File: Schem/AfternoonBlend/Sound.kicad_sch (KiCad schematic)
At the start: 56 parts, among them J4 STX-3120-3B, J5 Conn_01x03, U10 LM4880MX/NOPB, U11 SN76489AN, U12 SN76489AN, U2 TLV2372, U3 AD7801BRUZ, U6 SN76489AN, U7 SN76489AN, U8 74HC138, U9 74HCT21, Y1 ECS-2100A-035

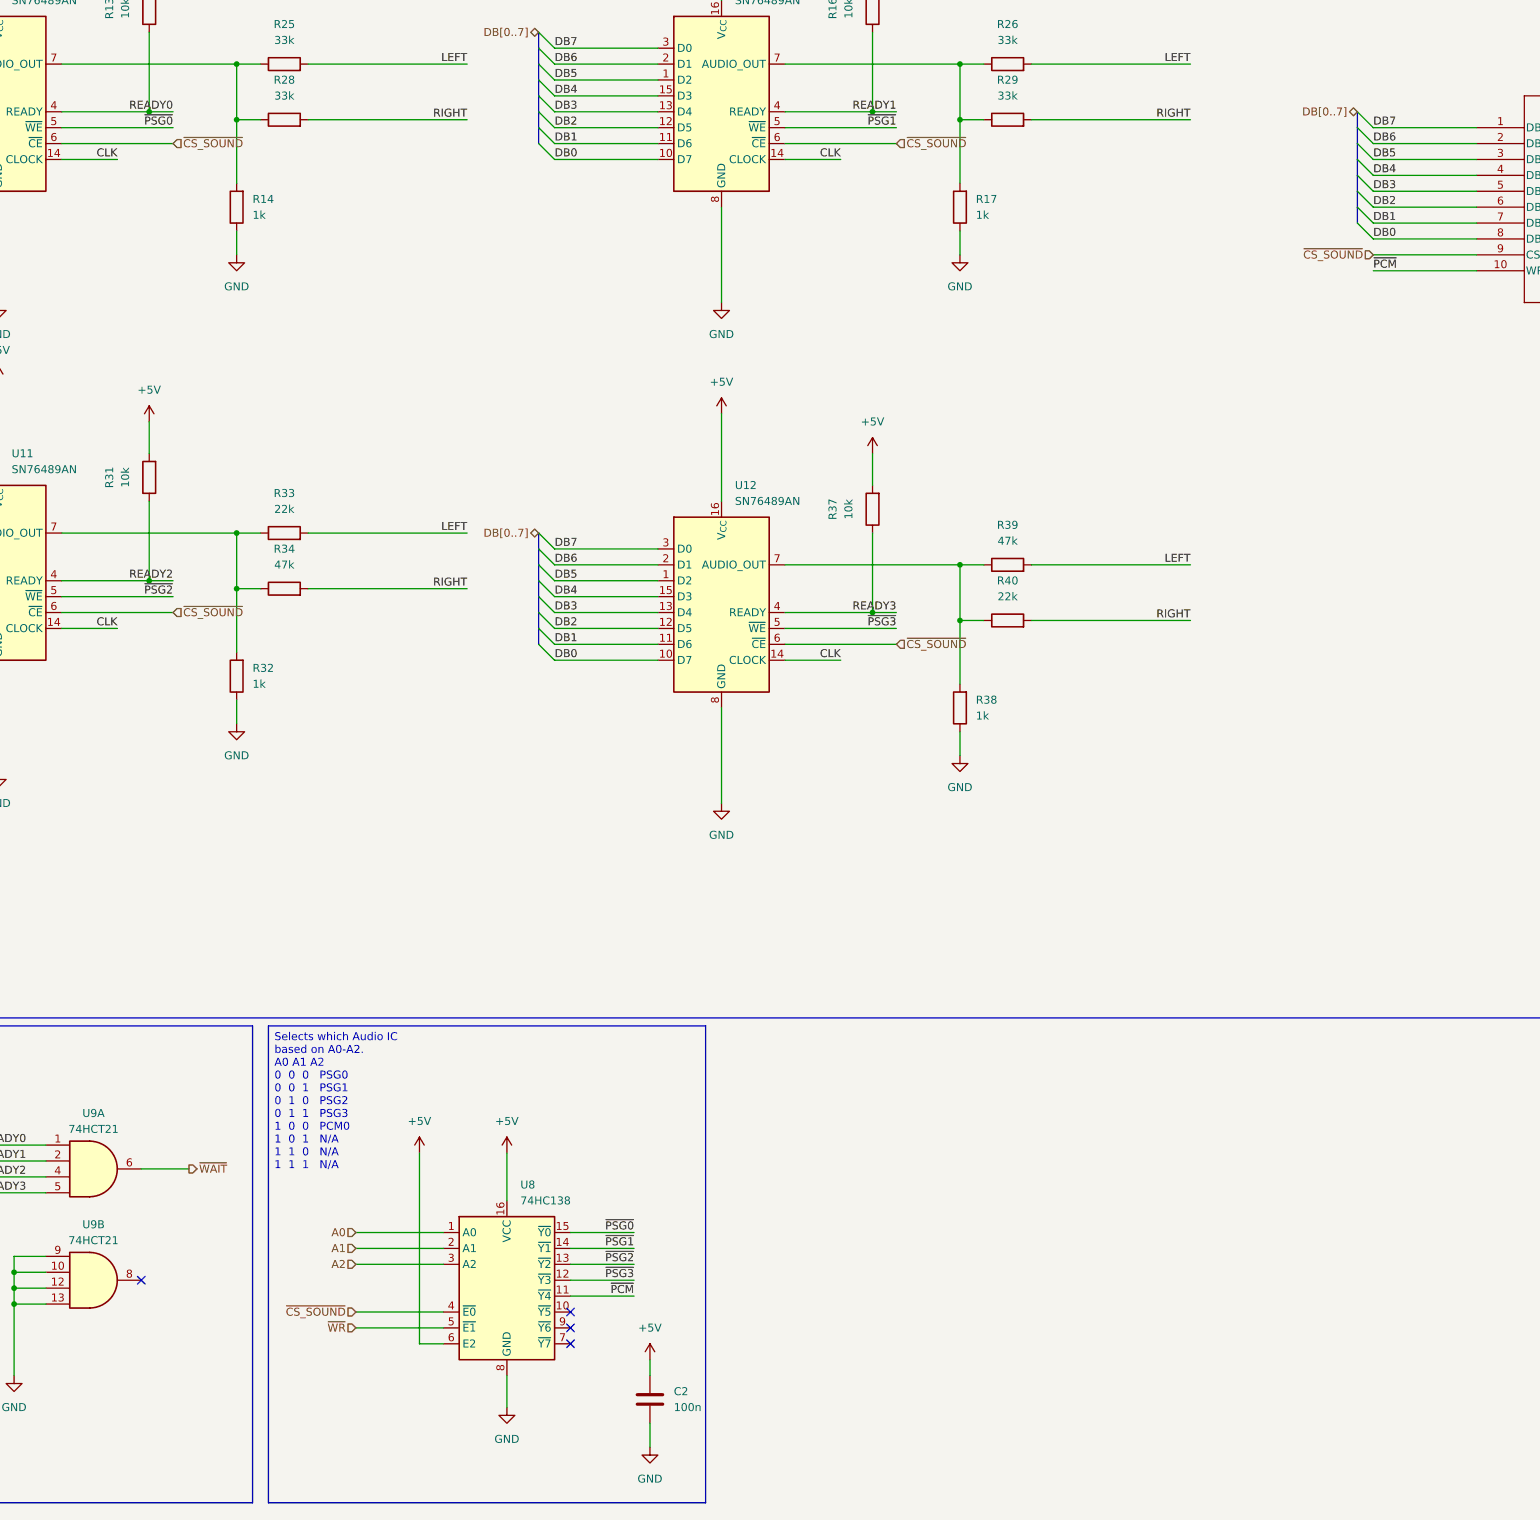
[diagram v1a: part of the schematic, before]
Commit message: Put back /CS_SOUND as the qualifying signal instead of /WR
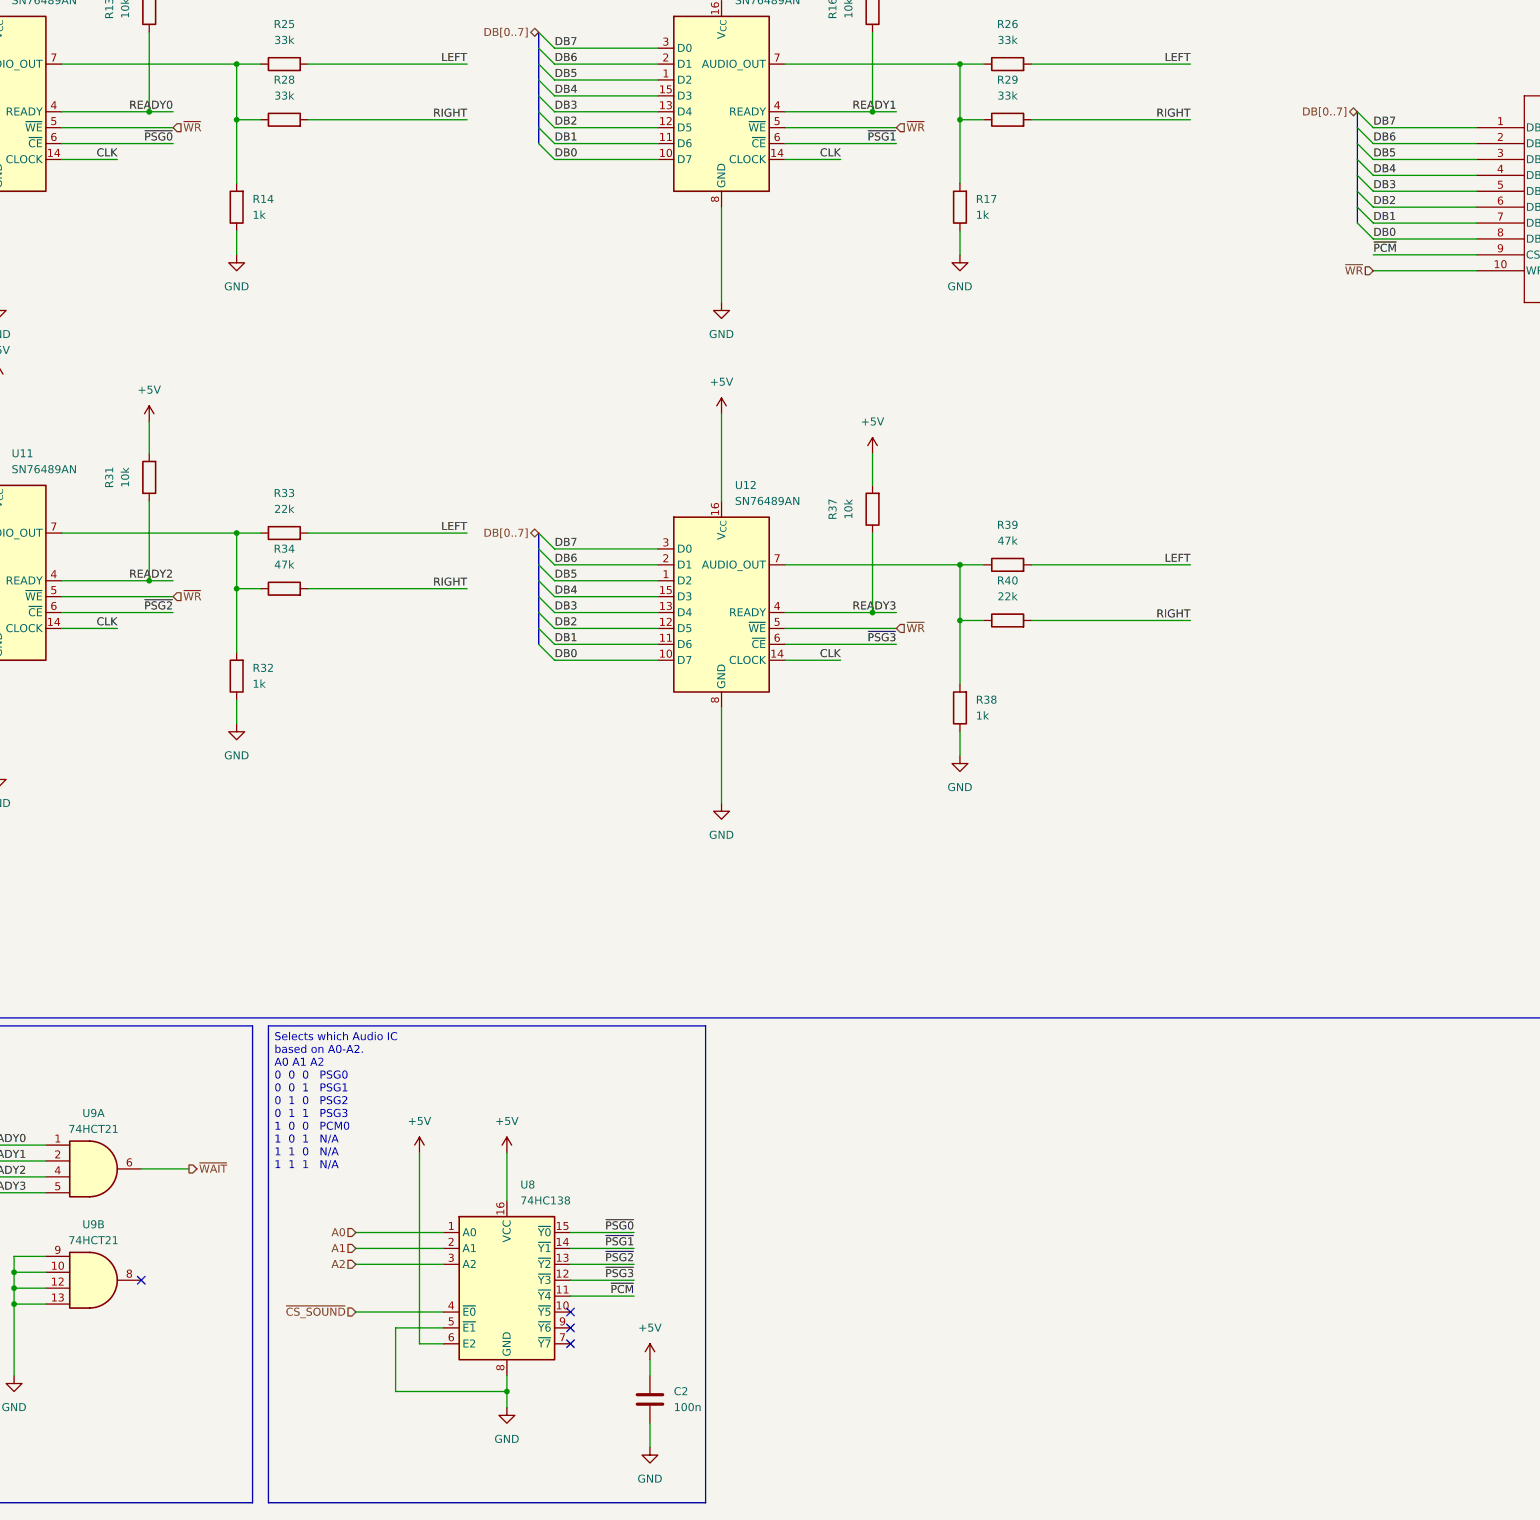
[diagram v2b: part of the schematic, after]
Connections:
- net GND: now also U8.5 (~{E1})
- net ~{CS_SOUND}: no longer U11.6 (~{CE}), U12.6 (~{CE}), U3.9 (CS*), U6.6 (~{CE}), U7.6 (~{CE})
- net ~{PCM}: now also U3.9 (CS*); no longer U3.10 (WR*)
- net ~{PSG0}: now also U6.6 (~{CE}); no longer U6.5 (~{WE})
- net ~{PSG1}: now also U7.6 (~{CE}); no longer U7.5 (~{WE})
- net ~{PSG2}: now also U11.6 (~{CE}); no longer U11.5 (~{WE})
- net ~{PSG3}: now also U12.6 (~{CE}); no longer U12.5 (~{WE})
- net ~{WR}: now also U11.5 (~{WE}), U12.5 (~{WE}), U3.10 (WR*), U6.5 (~{WE}), U7.5 (~{WE}); no longer U8.5 (~{E1})
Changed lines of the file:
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@@
 	)
 	(junction
+		(at 137.16 266.7)
+		(diameter 0)
+		(color 0 0 0 0)
+	)
+	(junction
 		(at 500.38 125.73)
 		(diameter 0)
@@
 		)
 	)
-	(wire
-		(pts
-			(xy 113.03 256.54) (xy 127 256.54)
-		)
-		(stroke
-			(width 0)
-			(type default)
-		)
-	)
 	(bus
 		(pts
@@
 	(wire
 		(pts
+			(xy 119.38 256.54) (xy 127 256.54)
+		)
+		(stroke
+			(width 0)
+			(type default)
+		)
+	)
+	(wire
+		(pts
 			(xy 450.85 167.64) (xy 458.47 167.64)
 		)
@@
 	(wire
 		(pts
-			(xy 137.16 264.16) (xy 137.16 269.24)
+			(xy 137.16 264.16) (xy 137.16 266.7)
 		)
 		(stroke
@@
 	(wire
 		(pts
+			(xy 137.16 266.7) (xy 137.16 269.24)
+		)
+		(stroke
+			(width 0)
+			(type default)
+		)
+	)
+	(wire
+		(pts
 			(xy 24.13 312.42) (xy 24.13 316.23)
 		)
@@
 	(wire
 		(pts
+			(xy 119.38 256.54) (xy 119.38 266.7)
+		)
+		(stroke
+			(width 0)
+			(type default)
+		)
+	)
+	(wire
+		(pts
 			(xy 181.61 147.32) (xy 199.39 147.32)
 		)
@@
 	(wire
 		(pts
+			(xy 119.38 266.7) (xy 137.16 266.7)
+		)
+		(stroke
+			(width 0)
+			(type default)
+		)
+	)
+	(wire
+		(pts
 			(xy 144.78 54.61) (xy 161.29 54.61)
 		)
@@
 		)
 	)
+	(label "~{PSG2}"
+		(at 83.82 142.24 180)
+		(effects
+			(font
+				(size 1.27 1.27)
+			)
+			(justify right bottom)
+		)
+	)
 	(label "DB6"
 		(at 144.78 54.61 0)
@@
 		)
 	)
-	(label "~{PSG2}"
-		(at 83.82 139.7 180)
-		(effects
-			(font
-				(size 1.27 1.27)
-			)
-			(justify right bottom)
-		)
-	)
 	(label "DB3"
 		(at 275.59 74.93 0)
@@
 		)
 	)
-	(label "~{PSG1}"
-		(at 199.39 64.77 180)
-		(effects
-			(font
-				(size 1.27 1.27)
-			)
-			(justify right bottom)
-		)
-	)
 	(label "LEFT"
 		(at 458.47 128.27 0)
@@
 		)
 	)
+	(label "~{PSG0}"
+		(at 83.82 67.31 180)
+		(effects
+			(font
+				(size 1.27 1.27)
+			)
+			(justify right bottom)
+		)
+	)
 	(label "DB4"
 		(at 29.21 59.69 0)
@@
 		)
 	)
-	(label "~{PSG3}"
-		(at 199.39 144.78 180)
-		(effects
-			(font
-				(size 1.27 1.27)
-			)
-			(justify right bottom)
-		)
-	)
 	(label "DB0"
 		(at 144.78 149.86 0)
@@
 		)
 	)
-	(label "~{PSG0}"
-		(at 83.82 64.77 180)
-		(effects
-			(font
-				(size 1.27 1.27)
-			)
-			(justify right bottom)
-		)
-	)
 	(label "DB0"
 		(at 29.21 69.85 0)
@@
 		)
 	)
+	(label "~{PSG3}"
+		(at 199.39 147.32 180)
+		(effects
+			(font
+				(size 1.27 1.27)
+			)
+			(justify right bottom)
+		)
+	)
 	(label "READY2"
 		(at 83.82 137.16 180)
@@
 		)
 	)
+	(label "~{PCM}"
+		(at 275.59 85.09 0)
+		(effects
+			(font
+				(size 1.27 1.27)
+			)
+			(justify left bottom)
+		)
+	)
+	(label "~{PSG1}"
+		(at 199.39 67.31 180)
+		(effects
+			(font
+				(size 1.27 1.27)
+			)
+			(justify right bottom)
+		)
+	)
 	(label "DB6"
 		(at 29.21 54.61 0)
@@
 		)
 	)
-	(label "~{PCM}"
-		(at 275.59 87.63 0)
-		(effects
-			(font
-				(size 1.27 1.27)
-			)
-			(justify left bottom)
-		)
-	)
 	(label "RIGHT"
 		(at 454.66 58.42 0)
@@
 		)
 	)
-	(hierarchical_label "~{WR}"
-		(shape input)
-		(at 113.03 256.54 180)
-		(effects
-			(font
-				(size 1.27 1.27)
-			)
-			(justify right)
-		)
-	)
 	(hierarchical_label "~{WAIT}"
 		(shape output)
@@
 		)
 	)
-	(hierarchical_label "~{CS_SOUND}"
+	(hierarchical_label "~{WR}"
 		(shape input)
-		(at 199.39 147.32 0)
+		(at 275.59 87.63 180)
 		(effects
 			(font
 				(size 1.27 1.27)
 			)
-			(justify left)
+			(justify right)
 		)
 	)
-	(hierarchical_label "~{CS_SOUND}"
+	(hierarchical_label "A1"
 		(shape input)
-		(at 83.82 67.31 0)
+		(at 113.03 243.84 180)
 		(effects
 			(font
 				(size 1.27 1.27)
 			)
-			(justify left)
+			(justify right)
 		)
 	)
-	(hierarchical_label "A1"
+	(hierarchical_label "~{WR}"
 		(shape input)
-		(at 113.03 243.84 180)
+		(at 199.39 64.77 0)
 		(effects
 			(font
 				(size 1.27 1.27)
 			)
-			(justify right)
+			(justify left)
 		)
 	)
@@
 		)
 	)
-	(hierarchical_label "~{CS_SOUND}"
-		(shape input)
-		(at 83.82 142.24 0)
-		(effects
-			(font
-				(size 1.27 1.27)
-			)
-			(justify left)
-		)
-	)
-	(hierarchical_label "~{CS_SOUND}"
+	(hierarchical_label "~{WR}"
 		(shape input)
-		(at 199.39 67.31 0)
+		(at 83.82 139.7 0)
 		(effects
 			(font
@@
 		)
 	)
+	(hierarchical_label "~{WR}"
+		(shape input)
+		(at 83.82 64.77 0)
+		(effects
+			(font
+				(size 1.27 1.27)
+			)
+			(justify left)
+		)
+	)
 	(hierarchical_label "DB[0..7]"
 		(shape bidirectional)
@@
 		)
 	)
-	(hierarchical_label "~{CS_SOUND}"
+	(hierarchical_label "~{WR}"
 		(shape input)
-		(at 275.59 85.09 180)
+		(at 199.39 144.78 0)
 		(effects
 			(font
 				(size 1.27 1.27)
 			)
-			(justify right)
+			(justify left)
 		)
 	)

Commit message: Added wait-state generation to cope with a 10MHz cpu
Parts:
- removed C18: 100n, Capacitor_SMD:C_0603_1608Metric, symbol Device:C
- removed R13, R16, R31, R37: 10k, Resistor_SMD:R_0603_1608Metric, symbol Device:R
- removed U9: 74HCT21, Package_SO:SOIC-14_3.9x8.7mm_P1.27mm, symbol 74xx:74LS21
- added C21, C22: 100n, Capacitor_SMD:C_0603_1608Metric, symbol Device:C
- added Q1: 2N7002, Package_TO_SOT_SMD:SOT-23, symbol Transistor_FET:2N7002
- added R15: 10k, Resistor_SMD:R_0603_1608Metric, symbol Device:R
- added R36: 47k, Resistor_SMD:R_0603_1608Metric, symbol Device:R
- added U5: 74AHCT74, Package_SO:TSSOP-14_4.4x5mm_P0.65mm, symbol 74xx:74HCT74
- added U9: 74AHCT00, Package_SO:TSSOP-14_4.4x5mm_P0.65mm, symbol 74xx:74HCT00
- C11, C12: MANUFACTURER_PART_NUMBER CL10B473KO8NNNC -> C0603C102K4RACTU
- R25, R26, R28, R29: MANUFACTURER_PART_NUMBER RC0603FR-0710KL -> RC0603FR-0733KL
- R33, R40: MANUFACTURER_PART_NUMBER RC0603FR-0710KL -> RC0603FR-0722KL
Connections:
- net READY1 is gone; now on net READY_ALL: U7.4 (READY)
- net READY2 is gone; now on net READY_ALL: U11.4 (READY)
- net READY3 is gone; now on net READY_ALL: U12.4 (READY)
- net +5V: now also C21.1, C22.1, R15.2, U5.10 (~{S}), U5.12 (D), U5.14 (VCC), U5.2 (D), U5.4 (~{S}), U9.14 (VCC)
- net GND: now also C21.2, C22.2, Q1.2 (S), R36.1, U5.7 (GND), U9.12, U9.13, U9.7 (GND)
- net ~{CS_SOUND}: now also U9.4, U9.5
- net ~{RESET}: now also U9.1
- net ~{WAIT}: now also Q1.3 (D)
- net READY0 renamed READY_ALL
- net READY_ALL: now also R15.1, U5.11 (C)
- new net CS_SOUND: U5.13 (~{R}), U5.3 (C), U9.6
- new net FF2_CLR: U9.10, U9.3, U9.9
- new net WAIT_GATE: Q1.1 (G), R36.2, U5.5 (Q)
- new net ~{FF2_CLR}: U5.1 (~{R}), U9.8
- new net ~{FF2_Q}: U5.8 (~{Q}), U9.2
- no-connect marks 5 -> 7
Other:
- moved on the sheet: C16, C17, C19, C5, C6, C7, C8

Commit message: Added WS Generator to sound card to match the speed of the CPU to the speed of the SN7 chips
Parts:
- added C23: 100n, Capacitor_SMD:C_0603_1608Metric, symbol Device:C
- added U14: 74AHC20, Package_SO:TSSOP-14_4.4x5mm_P0.65mm, symbol 74xx:74LS20
- R15: value 10k -> 2k2; MANUFACTURER_PART_NUMBER RC0603FR-0710KL -> RC0603FR-072K2L
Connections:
- net +5V: now also C23.1, U14.14 (VCC)
- net CS_SOUND: now also U14.6; no longer U9.6
- net GND: now also U9.4, U9.5, C23.2, U14.10, U14.12, U14.13, U14.7 (GND), U14.9; no longer U8.5 (~{E1})
- net ~{CS_SOUND}: no longer U9.4, U9.5
- net ~{PSG0}: now also U14.1
- net ~{PSG1}: now also U14.2
- net ~{PSG2}: now also U14.4
- net ~{PSG3}: now also U14.5
- net ~{WR}: now also U8.5 (~{E1})
- no-connect marks 7 -> 9
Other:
- moved on the sheet: C22, C3, U5C, U9D, U9E

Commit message: Fixed a couple of errors with the BOM
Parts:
- R19, R20, R21, R22: MANUFACTURER_PART_NUMBER RC0402FR-07100KL -> RC0603FR-07100KL
- R30, R34, R35, R36, R39: MANUFACTURER_PART_NUMBER CRRCR01FM47KS1 -> RC0603FR-0747KL
- U14: value 74AHC20 -> 74HC20
- U8: value 74HC138 -> 74AHCT138; MANUFACTURER_PART_NUMBER SN74HC138DR -> SN74AHCT138PWR
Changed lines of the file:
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@@
 			)
 		)
-		(property "MANUFACTURER_PART_NUMBER" "RC0402FR-07100KL"
+		(property "MANUFACTURER_PART_NUMBER" "RC0603FR-07100KL"
 			(at 580.39 66.04 90)
 			(hide yes)
@@
 			)
 		)
-		(property "Value" "74AHC20"
+		(property "Value" "74HC20"
 			(at 297.1703 182.88 0)
 			(show_name no)
@@
 			)
 		)
-		(property "MANUFACTURER_PART_NUMBER" "RC0402FR-07100KL"
+		(property "MANUFACTURER_PART_NUMBER" "RC0603FR-07100KL"
 			(at 450.85 175.26 90)
 			(hide yes)
@@
 			)
 		)
-		(property "MANUFACTURER_PART_NUMBER" "RC0402FR-07100KL"
+		(property "MANUFACTURER_PART_NUMBER" "RC0603FR-07100KL"
 			(at 580.39 142.24 90)
 			(hide yes)
@@
 			)
 		)
-		(property "MANUFACTURER_PART_NUMBER" "CRRCR01FM47KS1"
+		(property "MANUFACTURER_PART_NUMBER" "RC0603FR-0747KL"
 			(at 101.6 138.43 90)
 			(hide yes)
@@
 			)
 		)
-		(property "Value" "74AHC20"
+		(property "Value" "74HC20"
 			(at 297.1703 167.64 0)
 			(show_name no)
@@
 			)
 		)
-		(property "MANUFACTURER_PART_NUMBER" "CRRCR01FM47KS1"
+		(property "MANUFACTURER_PART_NUMBER" "RC0603FR-0747KL"
 			(at 388.62 78.74 0)
 			(hide yes)
@@
 			)
 		)
-		(property "MANUFACTURER_PART_NUMBER" "CRRCR01FM47KS1"
+		(property "MANUFACTURER_PART_NUMBER" "RC0603FR-0747KL"
 			(at 388.62 67.31 0)
 			(hide yes)
@@
 			)
 		)
-		(property "MANUFACTURER_PART_NUMBER" "CRRCR01FM47KS1"
+		(property "MANUFACTURER_PART_NUMBER" "RC0603FR-0747KL"
 			(at 332.74 143.51 0)
 			(hide yes)
@@
 			)
 		)
-		(property "MANUFACTURER_PART_NUMBER" "RC0402FR-07100KL"
+		(property "MANUFACTURER_PART_NUMBER" "RC0603FR-07100KL"
 			(at 462.28 167.64 90)
 			(hide yes)
@@
 			)
 		)
-		(property "MANUFACTURER_PART_NUMBER" "CRRCR01FM47KS1"
+		(property "MANUFACTURER_PART_NUMBER" "RC0603FR-0747KL"
 			(at 217.17 134.62 90)
 			(hide yes)
@@
 			)
 		)
-		(property "Value" "74HC138"
+		(property "Value" "74AHCT138"
 			(at 139.3033 236.22 0)
 			(show_name no)
@@
 			)
 		)
-		(property "MANUFACTURER_PART_NUMBER" "SN74HC138DR"
+		(property "MANUFACTURER_PART_NUMBER" "SN74AHCT138PWR"
 			(at 137.16 251.46 0)
 			(hide yes)
@@
 			)
 		)
-		(property "Value" "74AHC20"
+		(property "Value" "74HC20"
 			(at 44.45 253.9999 0)
 			(show_name no)

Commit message: updated the part #s
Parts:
- C11, C12: MANUFACTURER_PART_NUMBER C0603C102K4RACTU -> C0603C102J5GACTU
- Q1: MANUFACTURER_PART_NUMBER 2N7002 -> BSS138
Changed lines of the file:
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@@
 			)
 		)
-		(property "MANUFACTURER_PART_NUMBER" "2N7002"
+		(property "MANUFACTURER_PART_NUMBER" "BSS138"
 			(at 341.63 134.62 0)
 			(hide yes)
@@
 			)
 		)
-		(property "MANUFACTURER_PART_NUMBER" "C0603C102K4RACTU"
+		(property "MANUFACTURER_PART_NUMBER" "C0603C102J5GACTU"
 			(at 499.11 67.31 0)
 			(hide yes)
@@
 			)
 		)
-		(property "MANUFACTURER_PART_NUMBER" "C0603C102K4RACTU"
+		(property "MANUFACTURER_PART_NUMBER" "C0603C102J5GACTU"
 			(at 500.38 137.16 0)
 			(hide yes)
